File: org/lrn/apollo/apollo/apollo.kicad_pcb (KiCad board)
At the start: 2 copper layers, 44 parts, among them J1 Conn_01x01_Male, J2 Conn_01x01_Male, J3 Conn_01x01_Male, J4 Conn_01x01_Male, Q1 PN2222A, Q2 PN2222A, Q3 PN2222A, Q4 PN2222A, U1 74HC595, U2 5461AS-1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

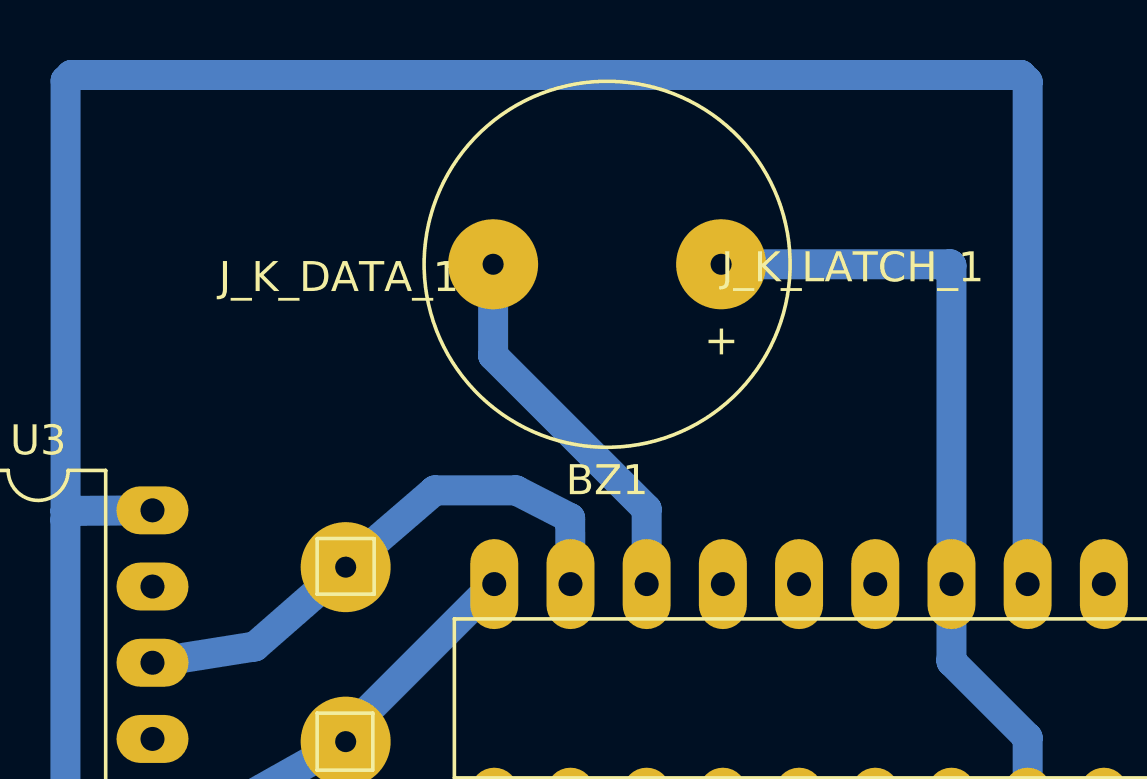
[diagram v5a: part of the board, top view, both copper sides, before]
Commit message: apollo: add beep LED signalization to scheme
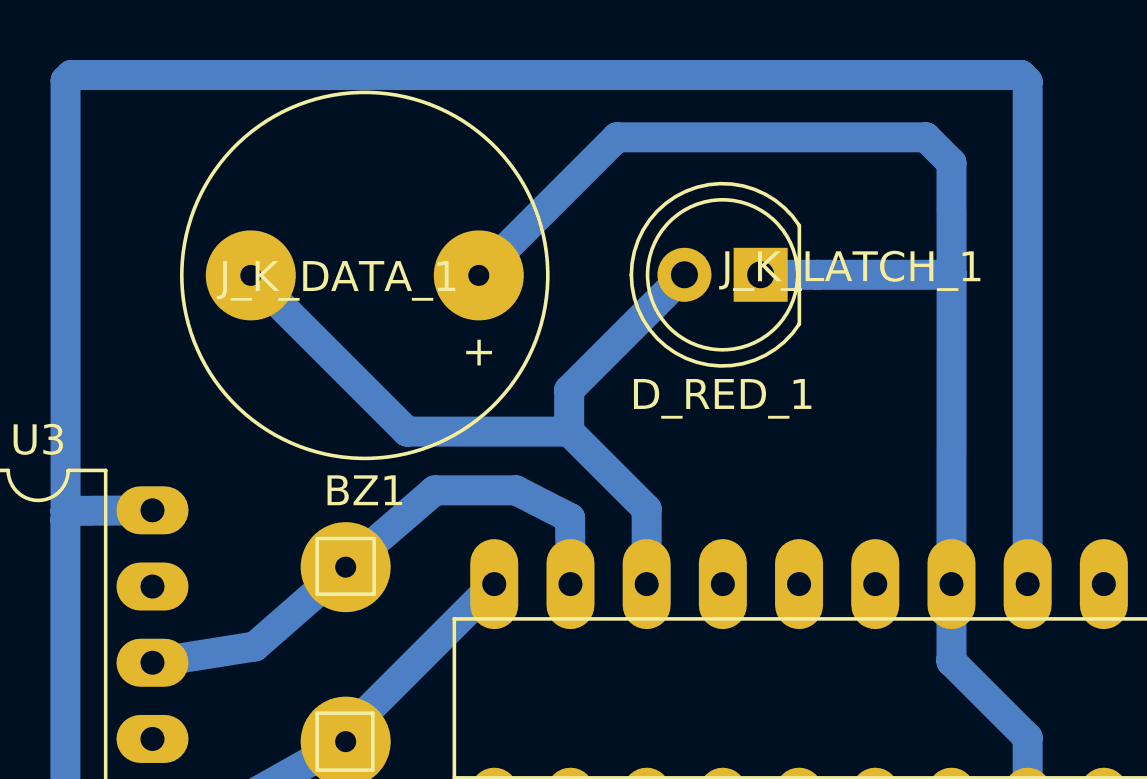
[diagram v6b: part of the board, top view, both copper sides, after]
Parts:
- added D_RED_1: LED, LED_THT:LED_D5.0mm_FlatTop, F.Cu at (154.9, 28.5)
- moved BZ1 8.09 mm to (145.5, 28.5)
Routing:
- net GND: track 245.8 -> 265.9 mm
- net Net-(BZ1-Pad2): track 12.8 -> 25.7 mm
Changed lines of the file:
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@@
     (thickness 1.6)
     (drawings 0)
-    (tracks 248)
+    (tracks 255)
     (zones 0)
-    (modules 44)
+    (modules 45)
     (nets 62)
   )
@@
   )
   (module Buzzer_Beeper:Buzzer_12x9.5RM7.6 (layer F.Cu)
-    (at 153.53538 28.10002 180)
+    (at 145.45818 28.47086 180)
     (descr "Generic Buzzer, D12mm height 9.5mm with RM7.6mm")
     (tags buzzer)
@@
       (net 60 "Net-(BZ1-Pad2)"))
     (model ${KISYS3DMOD}/Buzzer_Beeper.3dshapes/Buzzer_12x9.5RM7.6.wrl
+      (at (xyz 0 0 0))
+      (scale (xyz 1 1 1))
+      (rotate (xyz 0 0 0))
+    )
+  )
+  (module LED_THT:LED_D5.0mm_FlatTop (layer F.Cu)
+    (at 154.85364 28.45054 180)
+    (descr "LED, Round, FlatTop, diameter 5.0mm, 2 pins, http://www.kingbright.com/attachments/file/psearch/000/00/00/L-483GDT(Ver.15B).pdf")
+    (tags "LED Round FlatTop diameter 5.0mm 2 pins")
+    (fp_text reference D_RED_1 (at 1.27 -4.01) (layer F.SilkS)
+      (effects (font (size 1 1) (thickness 0.15)))
+    )
+    (fp_text value LED (at 1.27 4.01) (layer F.Fab)
+      (effects (font (size 1 1) (thickness 0.15)))
+    )
+    (fp_arc (start 1.27 0) (end -1.23 -1.566046) (angle 295.9) (layer F.Fab) (width 0.1))
+    (fp_arc (start 1.27 0) (end -1.29 -1.639512) (angle 147.4) (layer F.SilkS) (width 0.12))
+    (fp_arc (start 1.27 0) (end -1.29 1.639512) (angle -147.4) (layer F.SilkS) (width 0.12))
+    (fp_circle (center 1.27 0) (end 3.77 0) (layer F.Fab) (width 0.1))
+    (fp_circle (center 1.27 0) (end 3.77 0) (layer F.SilkS) (width 0.12))
+    (fp_line (start -1.23 -1.566046) (end -1.23 1.566046) (layer F.Fab) (width 0.1))
+    (fp_line (start -1.29 -1.64) (end -1.29 1.64) (layer F.SilkS) (width 0.12))
+    (fp_line (start -2 -3.3) (end -2 3.3) (layer F.CrtYd) (width 0.05))
+    (fp_line (start -2 3.3) (end 4.55 3.3) (layer F.CrtYd) (width 0.05))
+    (fp_line (start 4.55 3.3) (end 4.55 -3.3) (layer F.CrtYd) (width 0.05))
+    (fp_line (start 4.55 -3.3) (end -2 -3.3) (layer F.CrtYd) (width 0.05))
+    (pad 1 thru_hole rect (at 0 0 180) (size 1.8 1.8) (drill 0.9) (layers *.Cu *.Mask)
+      (net 30 GND))
+    (pad 2 thru_hole circle (at 2.54 0 180) (size 1.8 1.8) (drill 0.9) (layers *.Cu *.Mask)
+      (net 60 "Net-(BZ1-Pad2)"))
+    (model ${KISYS3DMOD}/LED_THT.3dshapes/LED_D5.0mm_FlatTop.wrl
       (at (xyz 0 0 0))
       (scale (xyz 1 1 1))
@@
   (segment (start 161.2138 41.3404) (end 161.2138 41.2604) (width 1) (layer B.Cu) (net 30))
   (segment (start 161.2138 41.2604) (end 161.2138 38.7604) (width 1) (layer B.Cu) (net 30))
-  (segment (start 153.53538 28.10002) (end 161.17316 28.10002) (width 1) (layer B.Cu) (net 30))
-  (segment (start 161.2138 28.14066) (end 161.2138 38.7604) (width 1) (layer B.Cu) (net 30))
-  (segment (start 161.17316 28.10002) (end 161.2138 28.14066) (width 1) (layer B.Cu) (net 30))
+  (segment (start 145.45818 28.47086) (end 150.06066 23.86838) (width 1) (layer B.Cu) (net 30))
+  (segment (start 150.06066 23.86838) (end 160.36544 23.86838) (width 1) (layer B.Cu) (net 30))
+  (segment (start 160.36544 23.86838) (end 161.2138 24.71674) (width 1) (layer B.Cu) (net 30))
+  (segment (start 156.75364 28.45054) (end 161.21888 28.45054) (width 1) (layer B.Cu) (net 30))
+  (segment (start 154.85364 28.45054) (end 156.75364 28.45054) (width 1) (layer B.Cu) (net 30))
+  (segment (start 161.21888 28.45054) (end 161.2138 38.7604) (width 1) (layer B.Cu) (net 30))
+  (segment (start 161.2138 24.71674) (end 161.21888 28.45054) (width 1) (layer B.Cu) (net 30))
   (segment (start 159.6136 129.5146) (end 159.59836 129.52984) (width 1) (layer B.Cu) (net 31))
   (segment (start 174.15416 129.5146) (end 159.6136 129.5146) (width 1) (layer B.Cu) (net 31))
@@
   (segment (start 141.0208 43.7134) (end 145.9738 38.7604) (width 1) (layer B.Cu) (net 59))
   (segment (start 141.0208 44.0122) (end 141.0208 43.7134) (width 1) (layer B.Cu) (net 59))
-  (segment (start 145.93538 31.14198) (end 145.93538 28.10002) (width 1) (layer B.Cu) (net 60))
-  (segment (start 151.0538 36.2604) (end 145.93538 31.14198) (width 1) (layer B.Cu) (net 60))
+  (segment (start 151.0538 36.2604) (end 148.47126 33.67786) (width 1) (layer B.Cu) (net 60))
   (segment (start 151.0538 38.7604) (end 151.0538 36.2604) (width 1) (layer B.Cu) (net 60))
+  (segment (start 143.06518 33.67786) (end 137.85818 28.47086) (width 1) (layer B.Cu) (net 60))
+  (segment (start 148.47126 33.67786) (end 143.06518 33.67786) (width 1) (layer B.Cu) (net 60))
+  (segment (start 148.47126 32.29292) (end 152.31364 28.45054) (width 1) (layer B.Cu) (net 60))
+  (segment (start 148.47126 33.67786) (end 148.47126 32.29292) (width 1) (layer B.Cu) (net 60))
 )

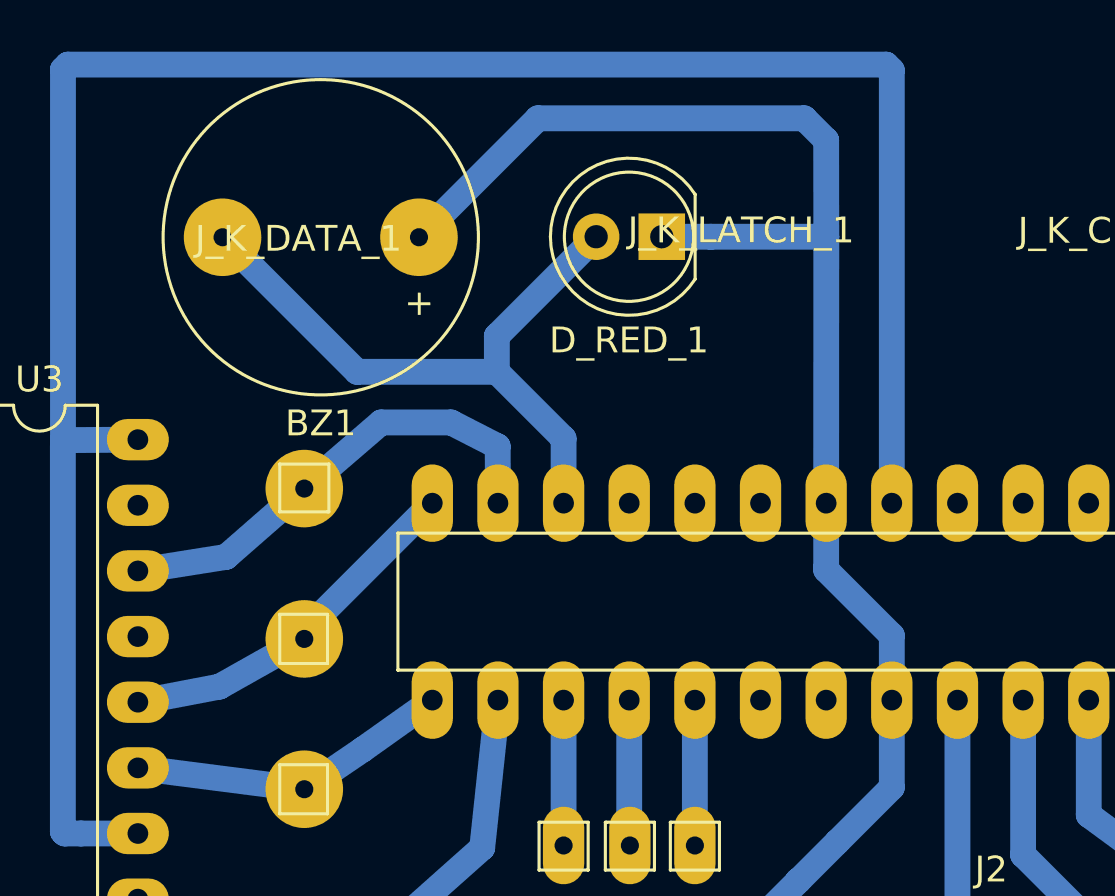
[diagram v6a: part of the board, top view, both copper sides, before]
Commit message: apollo: add R_LED for LED beeper in scheme
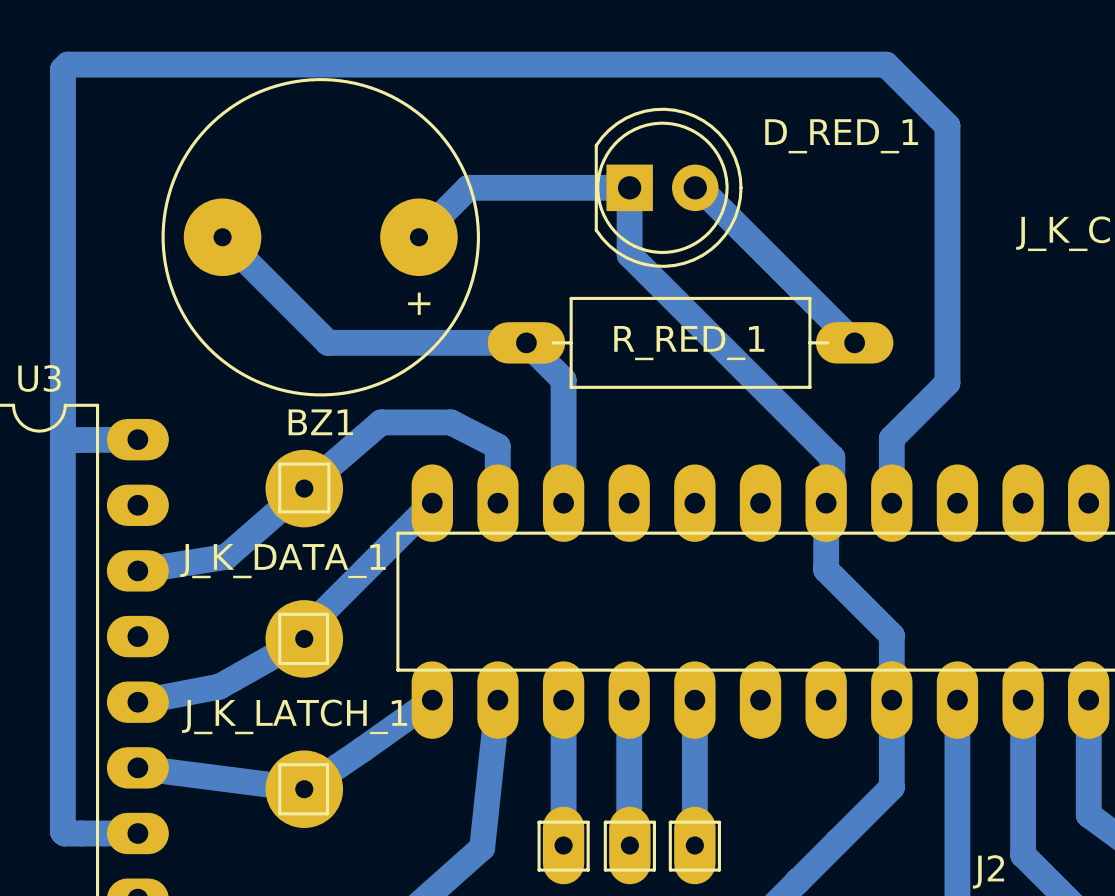
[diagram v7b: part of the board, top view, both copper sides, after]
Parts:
- added R_RED_1: R, apollo:R__Horizontal, F.Cu at (149.6, 32.6)
- moved D_RED_1 2.26 mm to (153.6, 26.6), turned to 0 degrees
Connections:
- D_RED_1 pad 2: Net-(BZ1-Pad2) -> Net-(D_RED_1-Pad2)
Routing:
- net GND: track 265.9 -> 252.0 mm
- net Net-(D_RED_1-Pad2): track 0.00 -> 8.65 mm
- net Net-(BZ1-Pad2): track 25.7 -> 20.2 mm
- net VCC: track 111.7 -> 113.5 mm

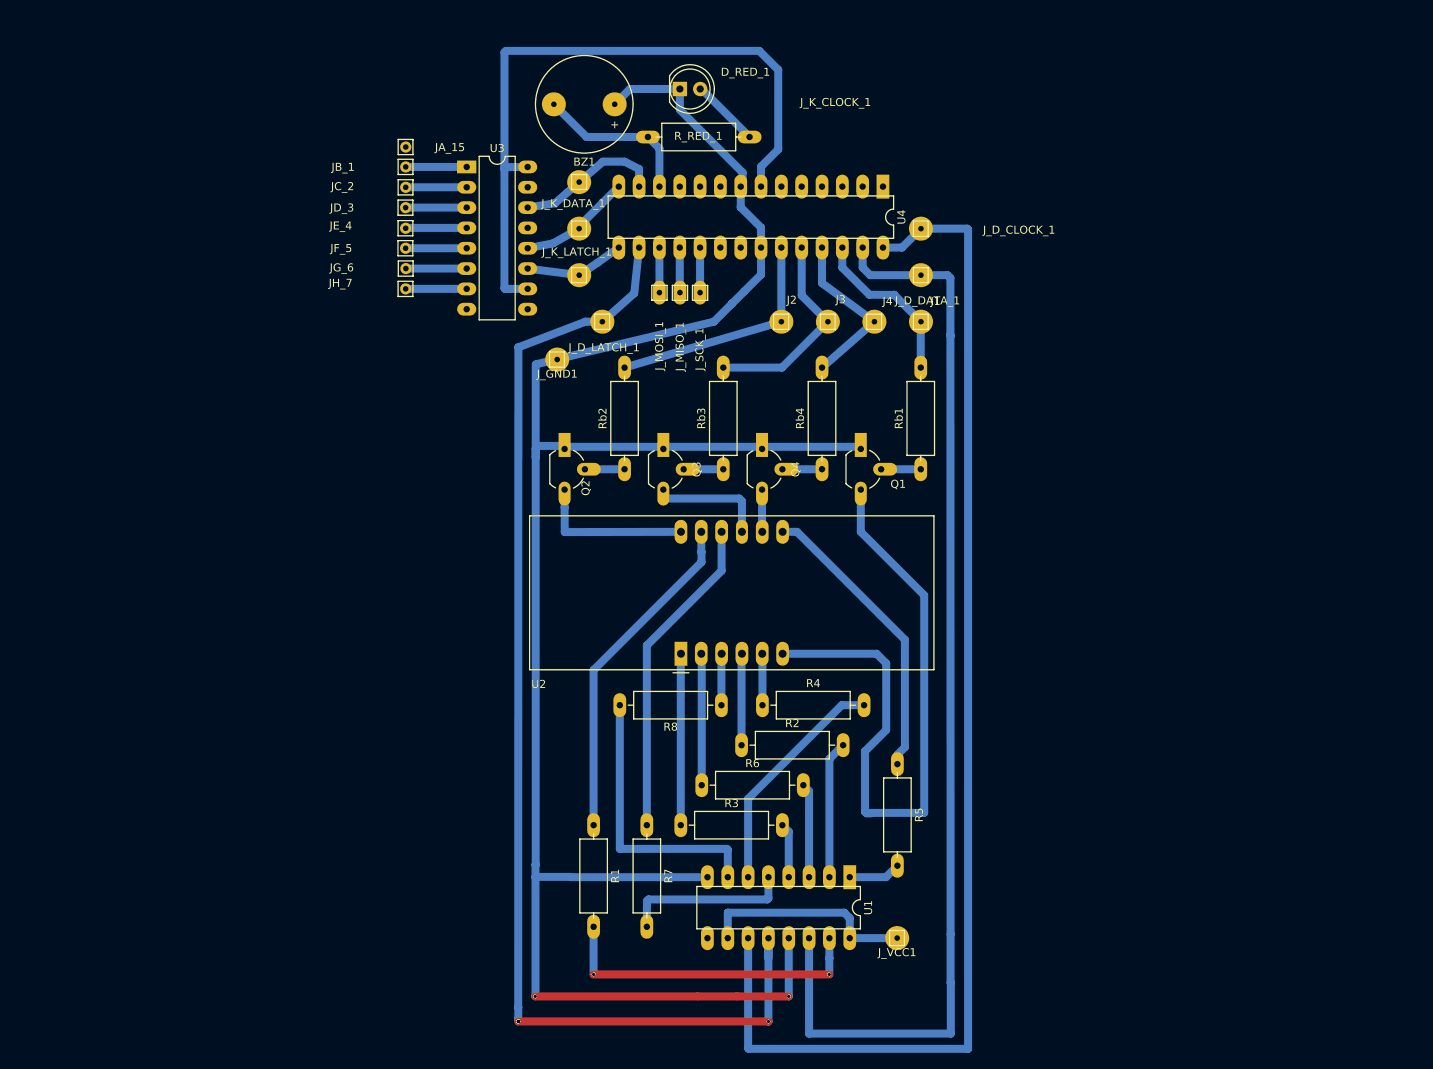
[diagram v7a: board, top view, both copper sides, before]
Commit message: apollo schematic: remove test contact pins
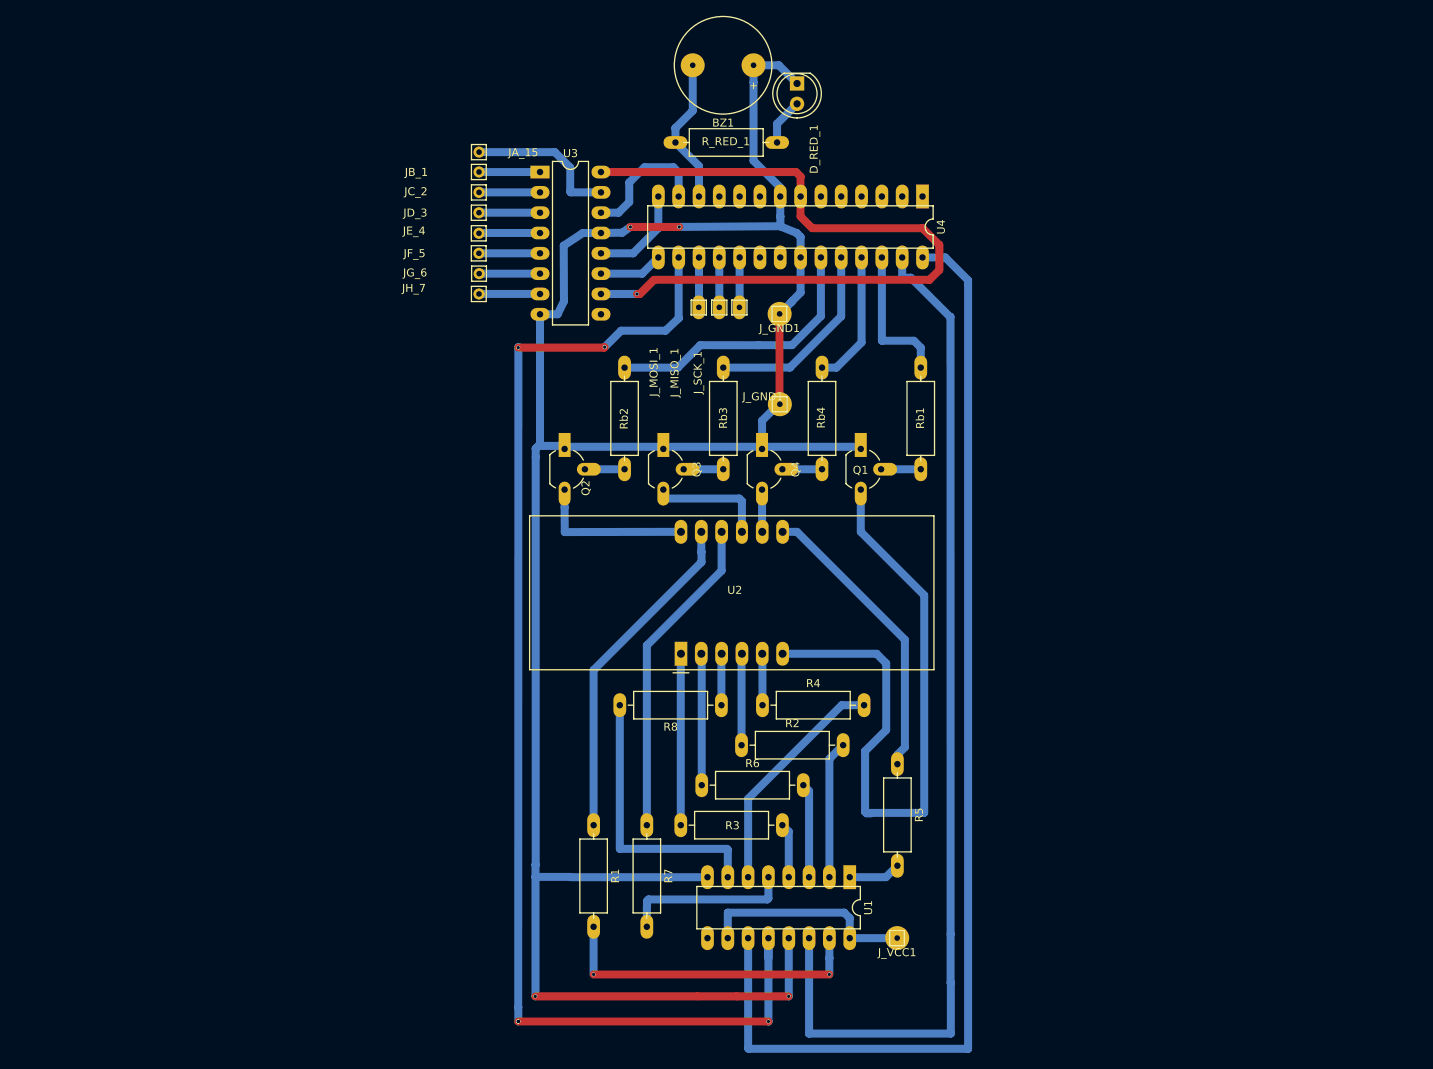
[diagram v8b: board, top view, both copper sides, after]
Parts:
- removed J1, J2, J3, J4, J_D_CLOCK_1, J_D_DATA_1, J_D_LATCH_1, J_K_CLOCK_1, J_K_DATA_1, J_K_LATCH_1: Conn_01x01_Male, Connector_Pin:Pin_D0.7mm_L6.5mm_W1.8mm_FlatFork
- removed the J_GND1 at (138.3, 60.4)
- added J_GND1: Conn_01x01_Male, Connector_Pin:Pin_D0.7mm_L6.5mm_W1.8mm_FlatFork, F.Cu at (166.1, 66.0)
- added J_GND1: Conn_01x01_Male, Connector_Pin:Pin_D0.7mm_L6.5mm_W1.8mm_FlatFork, F.Cu at (166.1, 54.7)
- moved BZ1 18.0 mm to (162.8, 23.6)
- moved D_RED_1 14.7 mm to (168.3, 25.9), turned to 270 degrees
- moved JB_1 9.19 mm to (128.5, 36.9)
- moved JC_2 9.19 mm to (128.5, 39.5)
- moved JF_5 9.19 mm to (128.5, 47.1)
- moved JG_6 9.19 mm to (128.5, 49.6)
- moved JH_7 9.19 mm to (128.5, 52.2)
- moved U3 9.19 mm to (136.1, 36.9)
- moved JA_15 9.19 mm to (128.5, 34.4)
- moved JD_3 9.19 mm to (128.5, 42.0)
- moved JE_4 9.19 mm to (128.5, 44.6)
- moved J_MISO_1 5.25 mm to (158.5, 53.8)
- moved J_MOSI_1 5.25 mm to (156.0, 53.8)
- moved J_SCK_1 5.25 mm to (161.0, 53.8)
- moved U4 5.09 mm to (183.9, 40.0)
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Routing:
- net GND: track 252.0 -> 287.3 mm, vias 2 -> 5
- net Net-(JA_15-Pad1): track 0.00 -> 19.1 mm
- net Net-(U1-Pad11): track 155.5 -> 144.3 mm
- net VCC: track 113.5 -> 123.1 mm, vias 0 -> 1
- net Net-(U1-Pad14): track 138.3 -> 129.9 mm
- net Net-(U1-Pad12): track 150.7 -> 157.8 mm, vias 3 -> 5
- net Net-(Rb2-Pad2): track 29.7 -> 34.6 mm
- net Net-(U3-Pad11): track 12.5 -> 8.01 mm
- net Net-(Rb4-Pad2): track 21.3 -> 16.9 mm
- net Net-(Rb1-Pad2): track 21.0 -> 18.1 mm
- net Net-(D_RED_1-Pad2): track 8.65 -> 5.87 mm
- net Net-(U3-Pad12): track 14.3 -> 12.4 mm
- net Net-(BZ1-Pad2): track 20.2 -> 18.5 mm
- net Net-(U3-Pad14): track 18.3 -> 16.8 mm
- net Net-(Rb3-Pad2): track 26.1 -> 24.7 mm
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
